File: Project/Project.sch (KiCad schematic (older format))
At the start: 44 parts, among them J1 Conn_01x05_Male, J2 USB_OTG, J3 Conn_01x09_Male, J4 Conn_01x03_Female, SW1 SW_Push, SW2 SW_Push, SW3 SW_Push, U1 CMWX1ZZABZ-078, U2 LM1117ADJ, U3 MCP73831-2-OT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

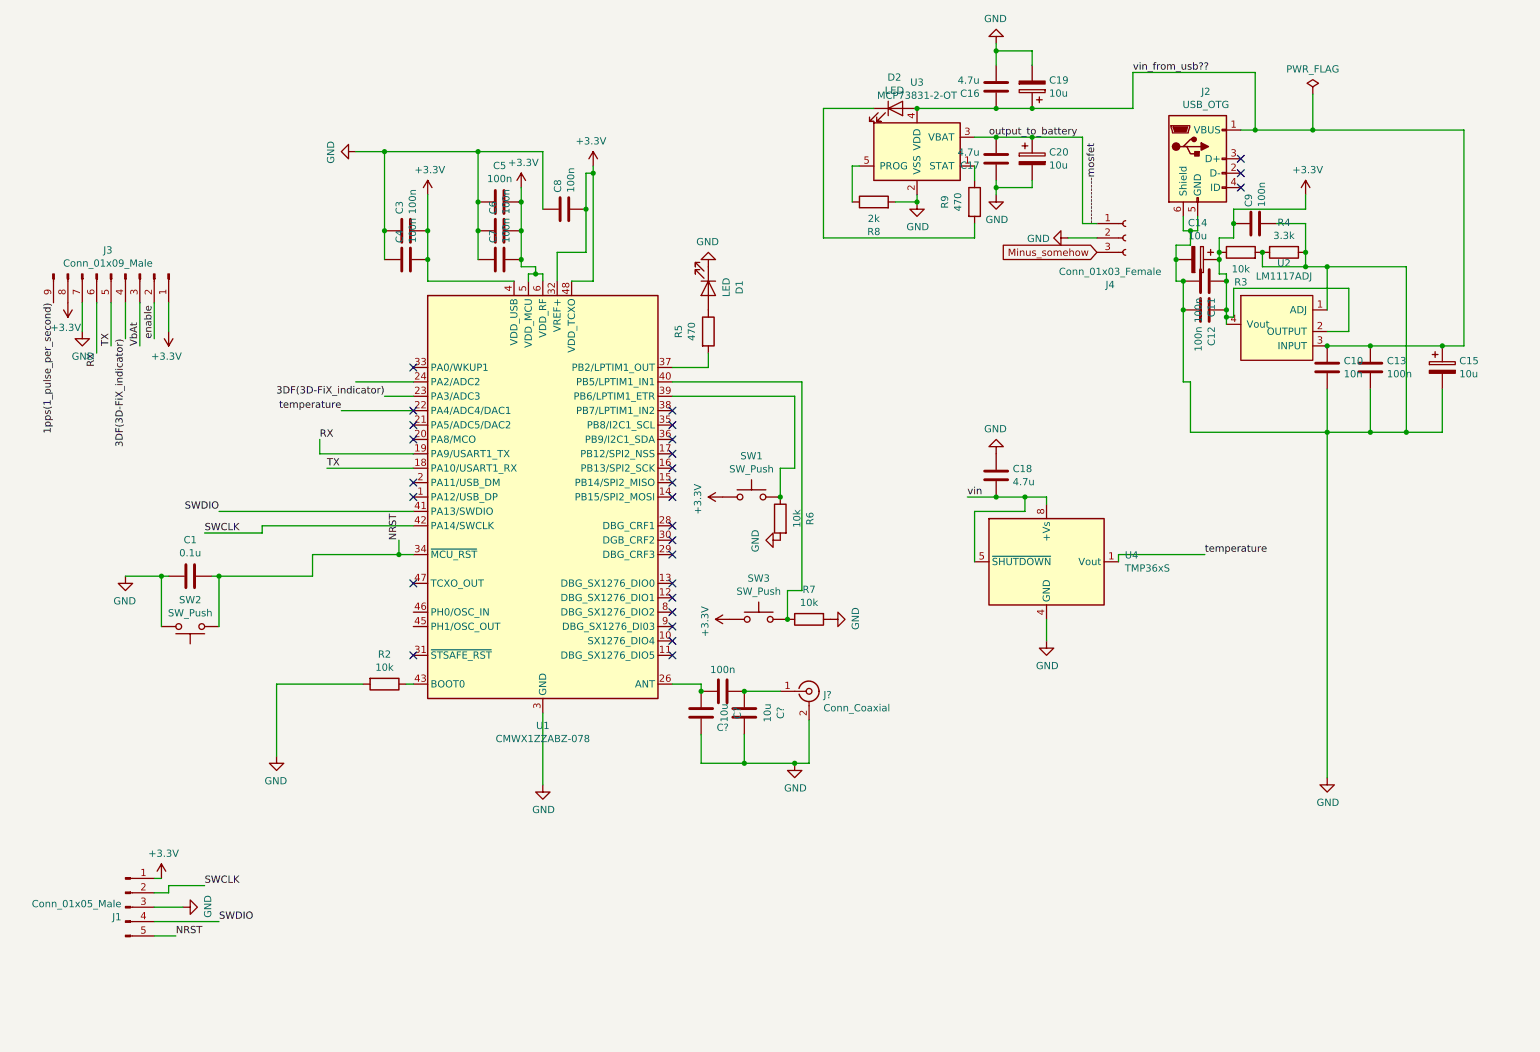
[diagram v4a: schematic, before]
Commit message: almost all footprints and schematic done
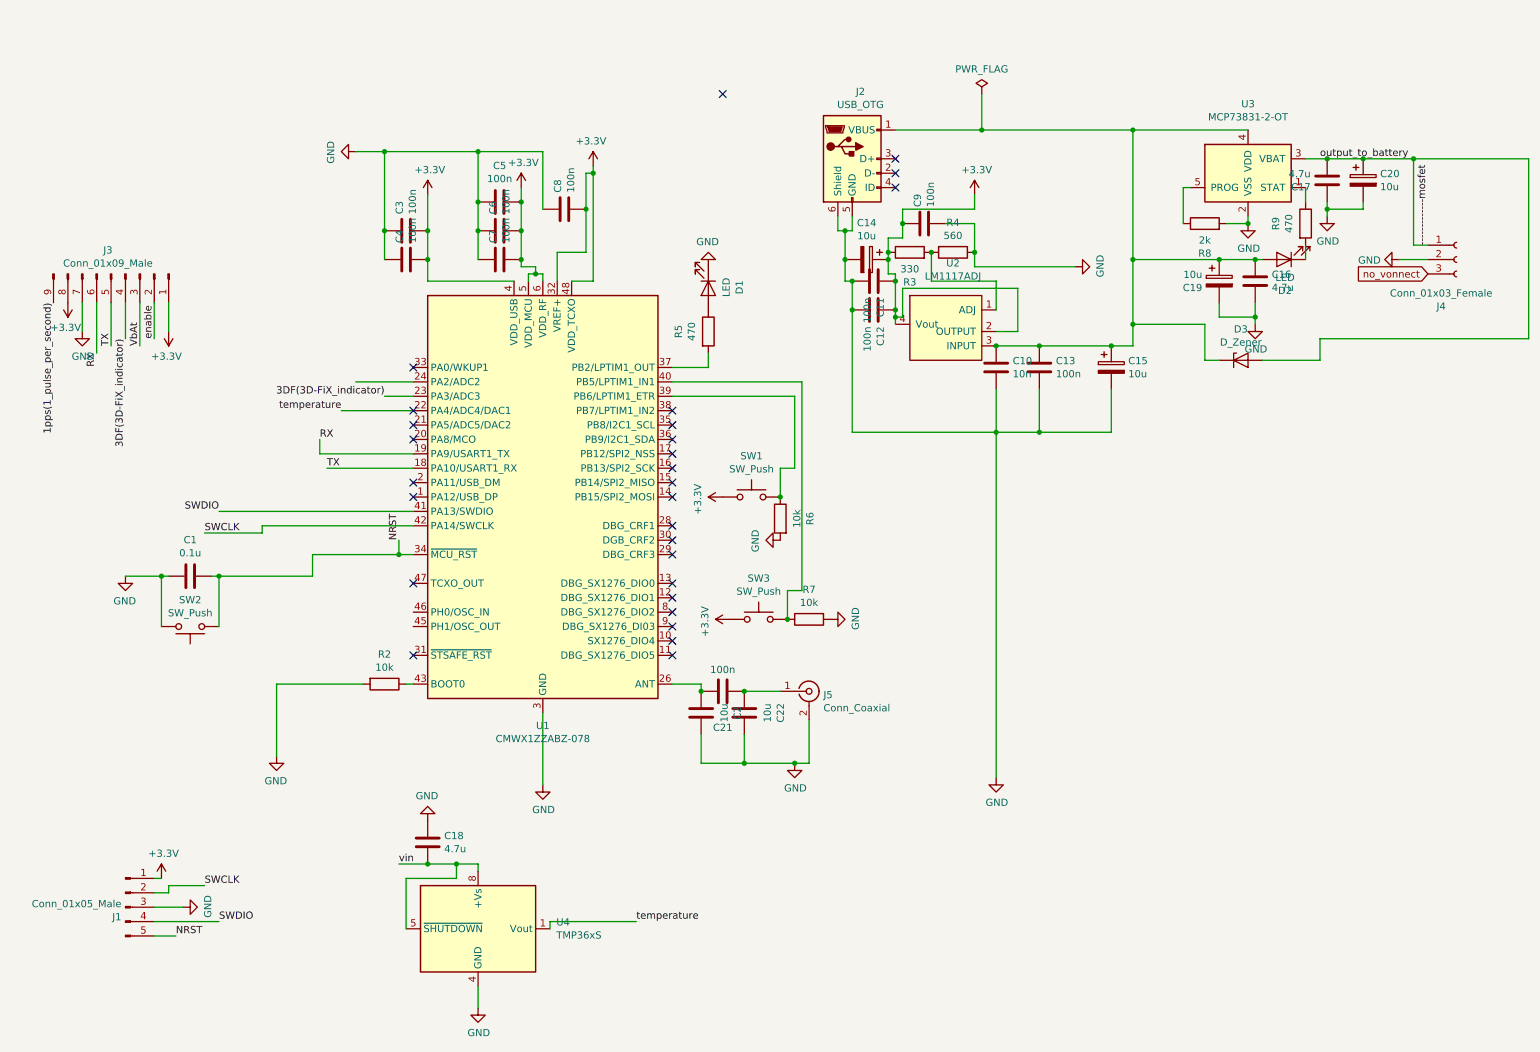
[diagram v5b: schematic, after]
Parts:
- added D3: D_Zener, Diode_SMD:D_0805_2012Metric_Pad1.15x1.40mm_HandSolder, symbol Device:D_Zener
- J2: footprint Connector_USB:USB_Mini-B_Wuerth_65100516121_Horizontal -> Connector_USB:USB_Micro-B_Wuerth_629105150521
- J4: footprint (none) -> Connector_JST:JST_PH_B3B-PH-K_1x03_P2.00mm_Vertical
- J5: renamed from J?; footprint (none) -> Connector_Coaxial:U.FL_Molex_MCRF_73412-0110_Vertical
- R3: value 10k -> 330
- R4: value 3.3k -> 560
- gave numbers to parts that had none: 3
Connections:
- net -------------mosfet: now also D3.2 (A)
- net GND: no longer R3.2, R4.2, U2.1 (ADJ)
- net Minus_somehow renamed no_vonnect
- net vin_from_usb??: no longer names the net of C10.1, C13.1, C15.1, C16.1, C19.1, D2.2 (A), J2.1 (VBUS), U2.3 (INPUT), U3.4 (VDD)
- net vin_from_usb??: now also D3.1 (K)
- new net: R3.2, R4.2, U2.1 (ADJ)
- no-connect marks 27 -> 28
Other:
- moved on the sheet: C10, C11, C12, C13, C14, C15, C16, C17, C18, C19, C20, C9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

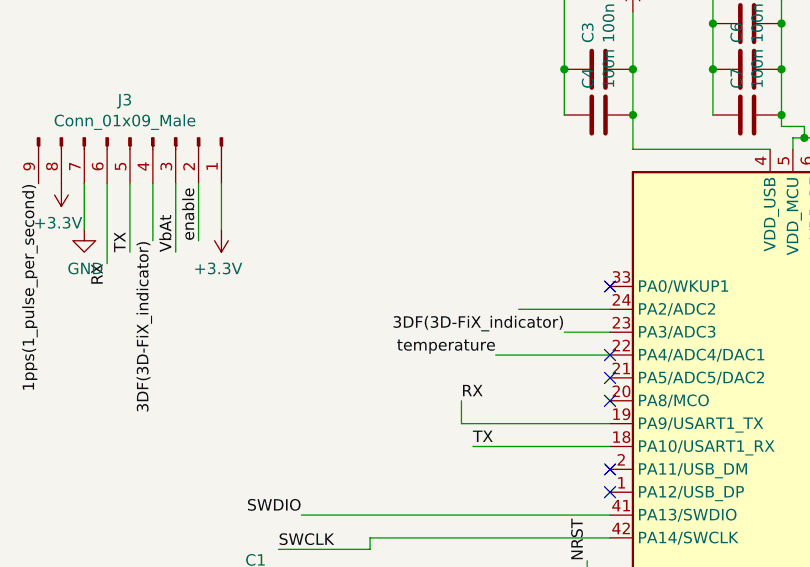
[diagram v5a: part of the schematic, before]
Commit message: almost all footprints and schematic done
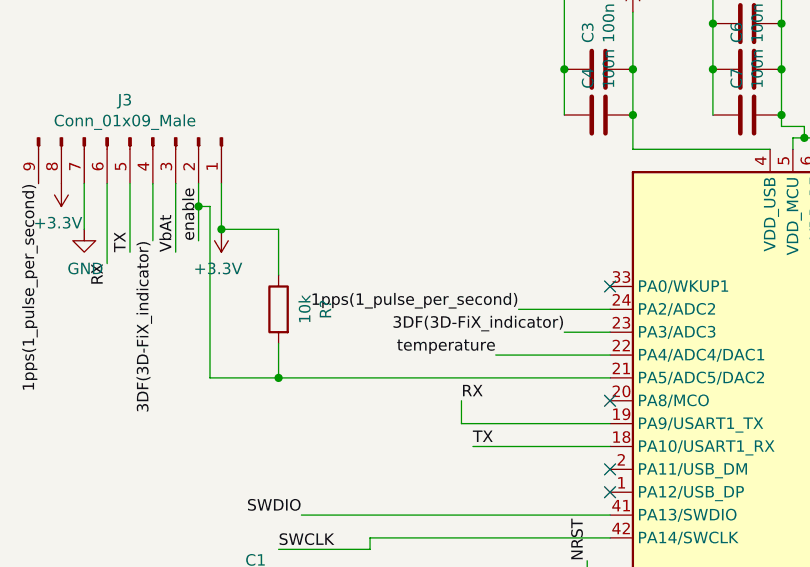
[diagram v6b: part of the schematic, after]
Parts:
- added R?: 10k, Resistor_SMD:R_0805_2012Metric_Pad1.15x1.40mm_HandSolder, symbol Device:R
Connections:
- net +3V3: now also R?.1
- net 1pps(1_pulse_per_second): now also U1.24 (PA2/ADC2)
- net enable: now also U1.21 (PA5/ADC5/DAC2), R?.2
- no-connect marks 28 -> 26
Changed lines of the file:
@@
 NoConn ~ 5150 3850
 NoConn ~ 3350 2950
-NoConn ~ 3350 3250
-NoConn ~ 3350 3350
 NoConn ~ 3350 3450
 NoConn ~ 3350 3750
@@
 enable
 Wire Wire Line
-	1550 2750 1550 2500
+	1550 2750 1550 2600
 Text Label 1450 2800 1    50   ~ 0
 VbAt
@@
 Wire Wire Line
 	9250 2900 9650 2900
+Text Label 2950 3050 2    50   ~ 0
+1pps(1_pulse_per_second)
+Wire Wire Line
+	1550 2600 1600 2600
+Connection ~ 1550 2600
+Wire Wire Line
+	1550 2600 1550 2500
+Wire Wire Line
+	1600 3350 1900 3350
+Wire Wire Line
+	1900 3350 1900 3200
+Wire Wire Line
+	1900 2700 1650 2700
+Connection ~ 1650 2700
+Wire Wire Line
+	1900 3350 3350 3350
+Connection ~ 1900 3350
+$Comp
+L Device:R R?
+U 1 1 5E71A4A3
+P 1900 3050
+F 0 "R?" V 1693 3050 50  0000 C CNN
+F 1 "10k" V 1784 3050 50  0000 C CNN
+F 2 "Resistor_SMD:R_0805_2012Metric_Pad1.15x1.40mm_HandSolder" V 1830 3050 50  0001 C CNN
+F 3 "~" H 1900 3050 50  0001 C CNN
+	1    1900 3050
+	-1   0    0    -1
+$EndComp
+Wire Wire Line
+	1900 2900 1900 2700
+Wire Wire Line
+	1600 2600 1600 3350
 $EndSCHEMATC

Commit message: some placements put
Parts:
- D3: footprint Diode_SMD:D_0805_2012Metric_Pad1.15x1.40mm_HandSolder -> Diode_SMD:D_SMA_Handsoldering
- gave numbers to parts that had none: 1
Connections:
- net vin is gone; now on net +3V3: C18.2, U4.5 (~SHUTDOWN), U4.8 (+Vs)
- net +3V3: no longer R1.1
- net enable: now also R1.1; no longer R1.2, U1.21 (PA5/ADC5/DAC2)
- net -------------mosfet: no longer names the net of C17.2, C20.1, D3.2 (A), J4.1 (Pin_1), U3.3 (VBAT)
- net no_vonnect: no longer names the net of J4.3 (Pin_3)
- new net: R1.2, U1.21 (PA5/ADC5/DAC2)
- no-connect marks 26 -> 31
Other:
- moved on the sheet: R1
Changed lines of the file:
@@
 L power:GND #PWR01
 U 1 1 5E2BBB8C
-P 4250 5850
-F 0 "#PWR01" H 4250 5600 50  0001 C CNN
-F 1 "GND" H 4255 5677 50  0000 C CNN
-F 2 "" H 4250 5850 50  0001 C CNN
-F 3 "" H 4250 5850 50  0001 C CNN
-	1    4250 5850
+P 4250 5650
+F 0 "#PWR01" H 4250 5400 50  0001 C CNN
+F 1 "GND" H 4255 5477 50  0000 C CNN
+F 2 "" H 4250 5650 50  0001 C CNN
+F 3 "" H 4250 5650 50  0001 C CNN
+	1    4250 5650
 	1    0    0    -1
 $EndComp
@@
 Wire Wire Line
 	4350 2150 4350 2350
-Wire Wire Line
-	4250 5350 4250 5850
 $Comp
 L power:GND #PWR0101
@@
 	9000 1950 9150 1950
 Wire Wire Line
-	9150 1950 9150 1900
-Wire Wire Line
 	8700 1950 8700 1700
 Wire Wire Line
@@
 	1    0    0    -1
 $EndComp
-Connection ~ 9150 1950
-Text Label 9650 1500 0    50   ~ 0
-output_to_battery
 $Comp
 L Device:C C17
@@
 	1    0    0    -1
 $EndComp
-Wire Wire Line
-	9700 1900 9700 1850
 Text Label 3150 3150 2    50   ~ 0
 3DF(3D-FiX_indicator)
@@
 	0    1    1    0
 $EndComp
-Wire Wire Line
-	10200 2200 10400 2200
-Text GLabel 10400 2300 0    50   Input ~ 0
-no_vonnect
 $Comp
 L Device:CP C20
@@
 Wire Wire Line
 	9950 1850 9700 1850
-Connection ~ 9700 1850
 Wire Wire Line
 	9700 1850 9700 1800
@@
 Text Label 1550 2750 1    50   ~ 0
 enable
-Wire Wire Line
-	1550 2750 1550 2600
 Text Label 1450 2800 1    50   ~ 0
 VbAt
@@
 	-1   0    0    1
 $EndComp
-Text Label 3250 6400 0    50   ~ 0
-vin
-Wire Wire Line
-	3250 6400 3450 6400
+Wire Wire Line
+	3250 6400 3300 6400
 Wire Wire Line
 	3800 6400 3800 6450
@@
 Wire Wire Line
 	3650 6400 3800 6400
-Text Label 10400 2100 1    50   ~ 0
--------------mosfet
 Connection ~ 8950 2200
 Wire Wire Line
@@
 Wire Wire Line
 	7250 2250 7950 2250
-Wire Wire Line
-	7400 2550 7400 2350
-Wire Wire Line
-	7400 2350 6950 2350
-Wire Wire Line
-	6950 2350 6950 2150
-Connection ~ 6950 2150
 $Comp
 L Device:D_Zener D3
@@
 F 0 "D3" H 9100 3116 50  0000 C CNN
 F 1 "D_Zener" H 9100 3025 50  0000 C CNN
-F 2 "Diode_SMD:D_0805_2012Metric_Pad1.15x1.40mm_HandSolder" H 9100 2900 50  0001 C CNN
+F 2 "Diode_SMD:D_SMA_Handsoldering" H 9100 2900 50  0001 C CNN
 F 3 "~" H 9100 2900 50  0001 C CNN
 	1    9100 2900
@@
 Text Label 2950 3050 2    50   ~ 0
 1pps(1_pulse_per_second)
-Wire Wire Line
-	1550 2600 1600 2600
-Connection ~ 1550 2600
-Wire Wire Line
-	1550 2600 1550 2500
-Wire Wire Line
-	1600 3350 1900 3350
-Wire Wire Line
-	1900 3350 1900 3200
-Wire Wire Line
-	1900 2700 1650 2700
-Connection ~ 1650 2700
-Wire Wire Line
-	1900 3350 3350 3350
-Connection ~ 1900 3350
-$Comp
-L Device:R R?
+$Comp
+L Device:R R1
 U 1 1 5E71A4A3
-P 1900 3050
-F 0 "R?" V 1693 3050 50  0000 C CNN
-F 1 "10k" V 1784 3050 50  0000 C CNN
-F 2 "Resistor_SMD:R_0805_2012Metric_Pad1.15x1.40mm_HandSolder" V 1830 3050 50  0001 C CNN
-F 3 "~" H 1900 3050 50  0001 C CNN
-	1    1900 3050
+P 1550 3050
+F 0 "R1" V 1343 3050 50  0000 C CNN
+F 1 "10k" V 1434 3050 50  0000 C CNN
+F 2 "Resistor_SMD:R_0805_2012Metric_Pad1.15x1.40mm_HandSolder" V 1480 3050 50  0001 C CNN
+F 3 "~" H 1550 3050 50  0001 C CNN
+	1    1550 3050
 	-1   0    0    -1
 $EndComp
 Wire Wire Line
-	1900 2900 1900 2700
-Wire Wire Line
-	1600 2600 1600 3350
+	1550 3350 1550 3200
+Wire Wire Line
+	1550 3350 3350 3350
+Wire Wire Line
+	1550 2500 1550 2900
+NoConn ~ 1450 2800
+NoConn ~ 1450 2500
+Wire Wire Line
+	9700 1850 9700 1900
+Connection ~ 9700 1850
+NoConn ~ 3350 4650
+NoConn ~ 3350 4750
+Wire Wire Line
+	9150 1900 9150 1950
+Connection ~ 9150 1950
+Wire Wire Line
+	6950 2150 6950 2350
+Wire Wire Line
+	6950 2350 7450 2350
+Wire Wire Line
+	7450 2350 7450 2550
+Wire Wire Line
+	7450 2550 7400 2550
+Connection ~ 6950 2150
+$Comp
+L power:+3.3V #PWR0126
+U 1 1 5E4DDA45
+P 3300 6400
+F 0 "#PWR0126" H 3300 6250 50  0001 C CNN
+F 1 "+3.3V" H 3315 6573 50  0000 C CNN
+F 2 "" H 3300 6400 50  0001 C CNN
+F 3 "" H 3300 6400 50  0001 C CNN
+	1    3300 6400
+	0    -1   -1   0
+$EndComp
+Connection ~ 3300 6400
+Wire Wire Line
+	3300 6400 3450 6400
+NoConn ~ 10400 2300
+Wire Wire Line
+	4250 5650 4250 5350
+Wire Wire Line
+	10200 2200 10400 2200
 $EndSCHEMATC

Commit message: placed all components
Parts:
- C19, C20: footprint Capacitor_SMD:C_0805_2012Metric_Pad1.15x1.40mm_HandSolder -> Capacitor_SMD:CP_Elec_6.3x4.9
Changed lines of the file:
@@
 F 0 "C20" H 10068 1696 50  0000 L CNN
 F 1 "10u" H 10068 1605 50  0000 L CNN
-F 2 "Capacitor_SMD:C_0805_2012Metric_Pad1.15x1.40mm_HandSolder" H 9988 1500 50  0001 C CNN
+F 2 "Capacitor_SMD:CP_Elec_6.3x4.9" H 9988 1500 50  0001 C CNN
 F 3 "~" H 9950 1650 50  0001 C CNN
 	1    9950 1650
@@
 F 0 "C19" H 8832 2304 50  0000 R CNN
 F 1 "10u" H 8832 2395 50  0000 R CNN
-F 2 "Capacitor_SMD:C_0805_2012Metric_Pad1.15x1.40mm_HandSolder" H 8988 2200 50  0001 C CNN
+F 2 "Capacitor_SMD:CP_Elec_6.3x4.9" H 8988 2200 50  0001 C CNN
 F 3 "~" H 8950 2350 50  0001 C CNN
 	1    8950 2350
